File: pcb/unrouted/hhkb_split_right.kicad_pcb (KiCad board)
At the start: 2 copper layers, 173.7 x 97.4 mm, 83 parts, among them SW1 CPG151101S11-2, SW10 CPG151101S11-2, SW11 CPG151101S11-2, SW12 CPG151101S11-2, SW13 CPG151101S11-2, SW14 CPG151101S11-2, SW15 CPG151101S11-2, SW16 CPG151101S11-2, SW17 CPG151101S11-2, SW18 CPG151101S11-2, SW19 CPG151101S11-2, SW2 CPG151101S11-2, SW20 CPG151101S11-2, SW21 CPG151101S11-2, SW22 CPG151101S11-2, SW23 CPG151101S11-2, SW24 CPG151101S11-2, SW25 CPG151101S11-2, SW26 CPG151101S11-2, SW27 CPG151101S11-2, SW28 CPG151101S11-2, SW29 CPG151101S11-2, SW3 CPG151101S11-2, SW30 CPG151101S11-2, SW31 CPG151101S11-2, SW32 CPG151101S11-2, SW33 CPG151101S11-2, SW34 CPG151101S11-2, SW4 CPG151101S11-2, SW5 CPG151101S11-2, SW6 CPG151101S11-2, SW7 CPG151101S11-2, SW8 CPG151101S11-2, SW9 CPG151101S11-2, U1 74LVC595, U2 74LVC595

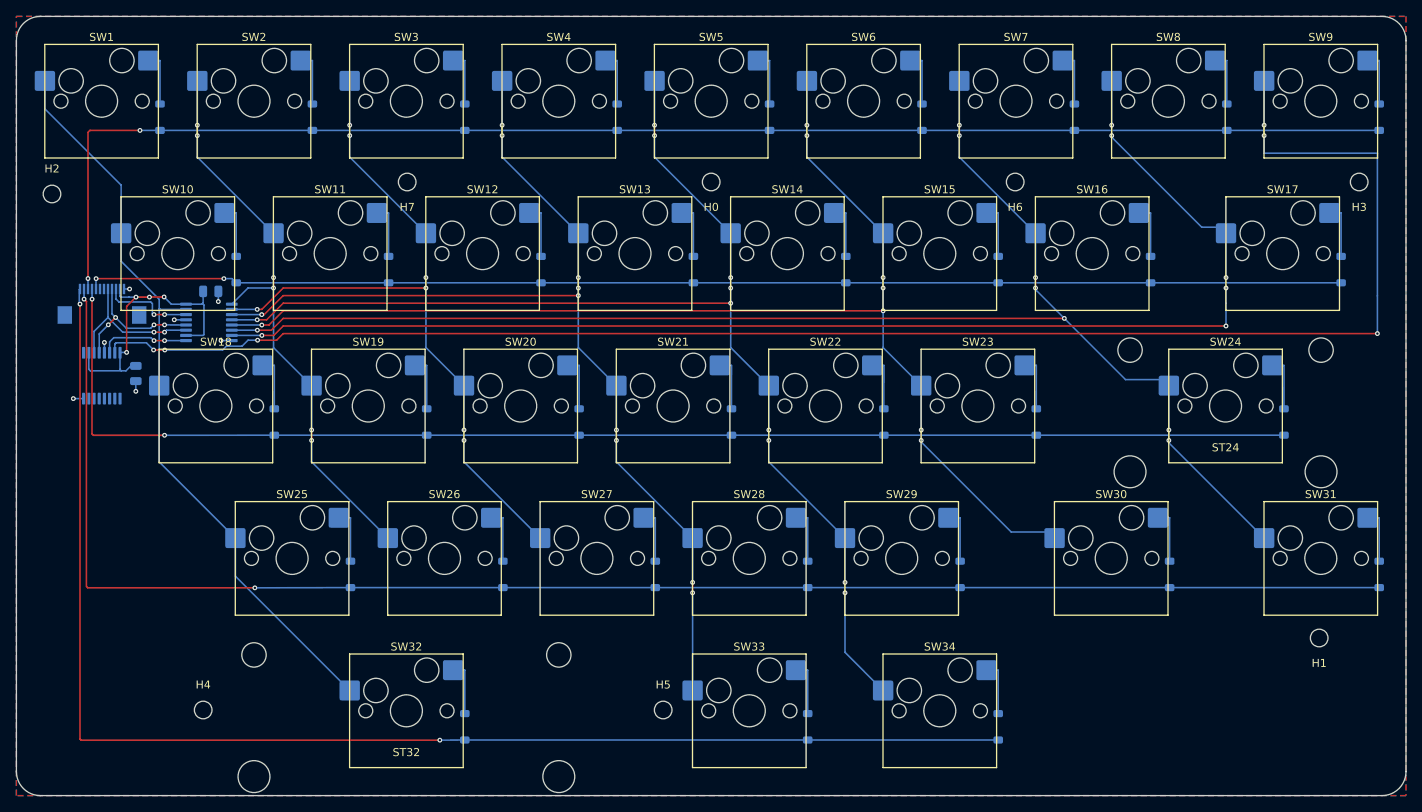
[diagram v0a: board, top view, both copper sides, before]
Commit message: #51 候補 3 を「右半分のみ」で実装した（PLATE_MARGIN_X_RIGHT = 3.125・幅 177.7mm）
利用者の採用決定を受けた実装。**左は実機のまま**——全幅で詰めると
電池（外壁基準）と子基板（内壁基準）が両側から近づき、左のアンテナ・
電池距離が 10.56→8.56mm で要件 10mm を割る（実装して発覚・巻き戻した）。
右の同距離は余裕 40mm で影響なし。実機からの逸脱も右半分だけになった。

- interface.py: 右専用余白＋margin_x()/margin_x_for_case()（キー幅 150mm/
  ケース幅 158mm を境に半分を判別。呼び出し元の変更を最小化）
- BEZEL_WALL 1.6→1.2・BEZEL_OPENING_GAP 1.5→0.9 は左右共通
  （見える隙間 1.225mm = 実機実測 1.0〜1.5 の範囲内）
- 検査: 余白の実機由来検査を左右別に・ベゼル幾何検査を両半分で実施・
  キャップ隙間の下限を実機実測の 1.0 に更新
- 右の新外形板を matrix_only に用意（利用者が J_DB 周り 9 ネットを引き直し中）
- 左基板・DRC 記録は凍結のまま無傷

検証: DRC 0/0/0（左右とも現行板で）・幾何/不変検査 138 件緑・
gen_assembly 左 干渉 0・全検査で残る赤は右基板系 3 件のみ
（旧外形の本番右板 vs 新定数。引き直し→finalize で解消する見込み）

Co-Authored-By: Claude Fable 5 <noreply@anthropic.com>
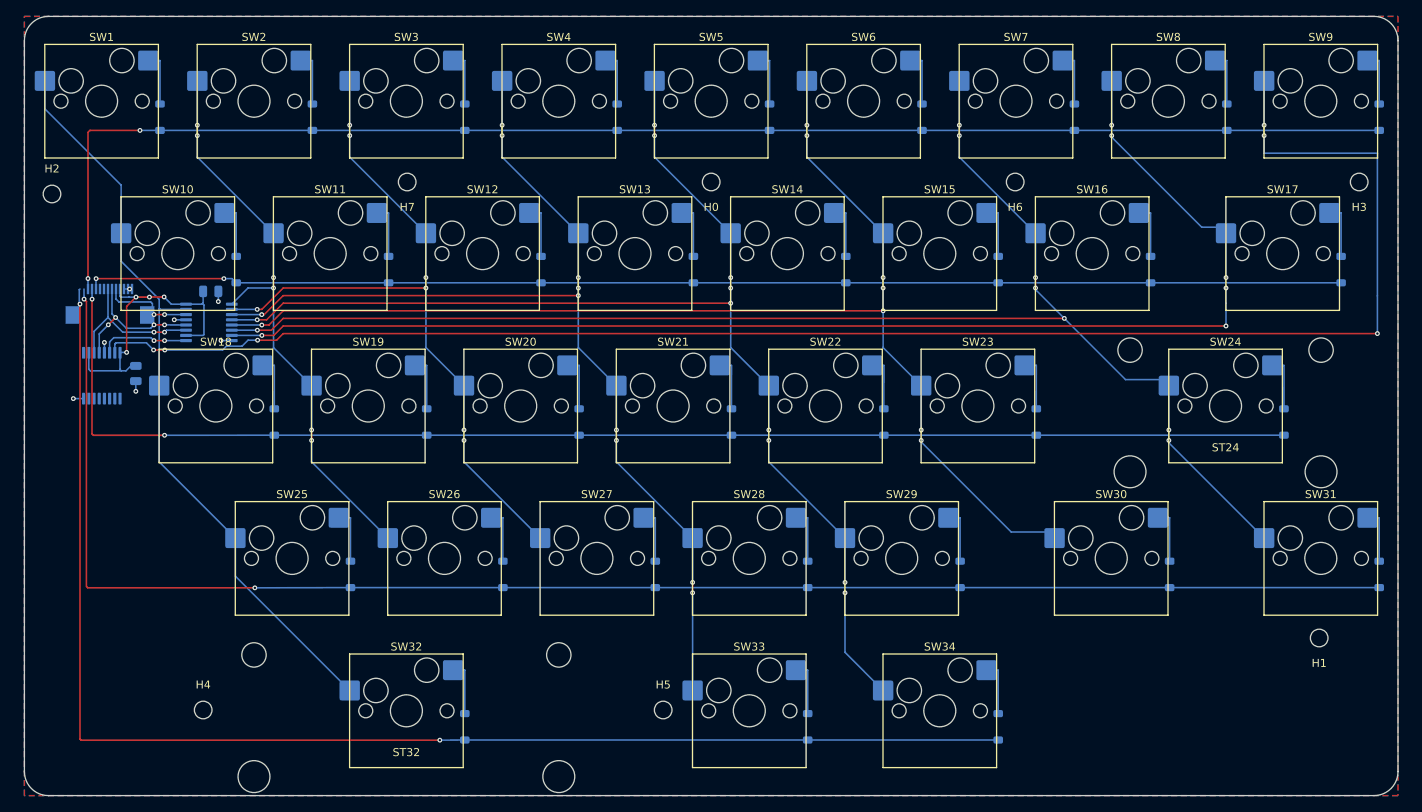
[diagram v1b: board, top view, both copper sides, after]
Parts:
- moved J_DB 1.00 mm to (74.8, 87.2)
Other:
- board size 173.7 x 97.4 mm -> 171.7 x 97.4 mm

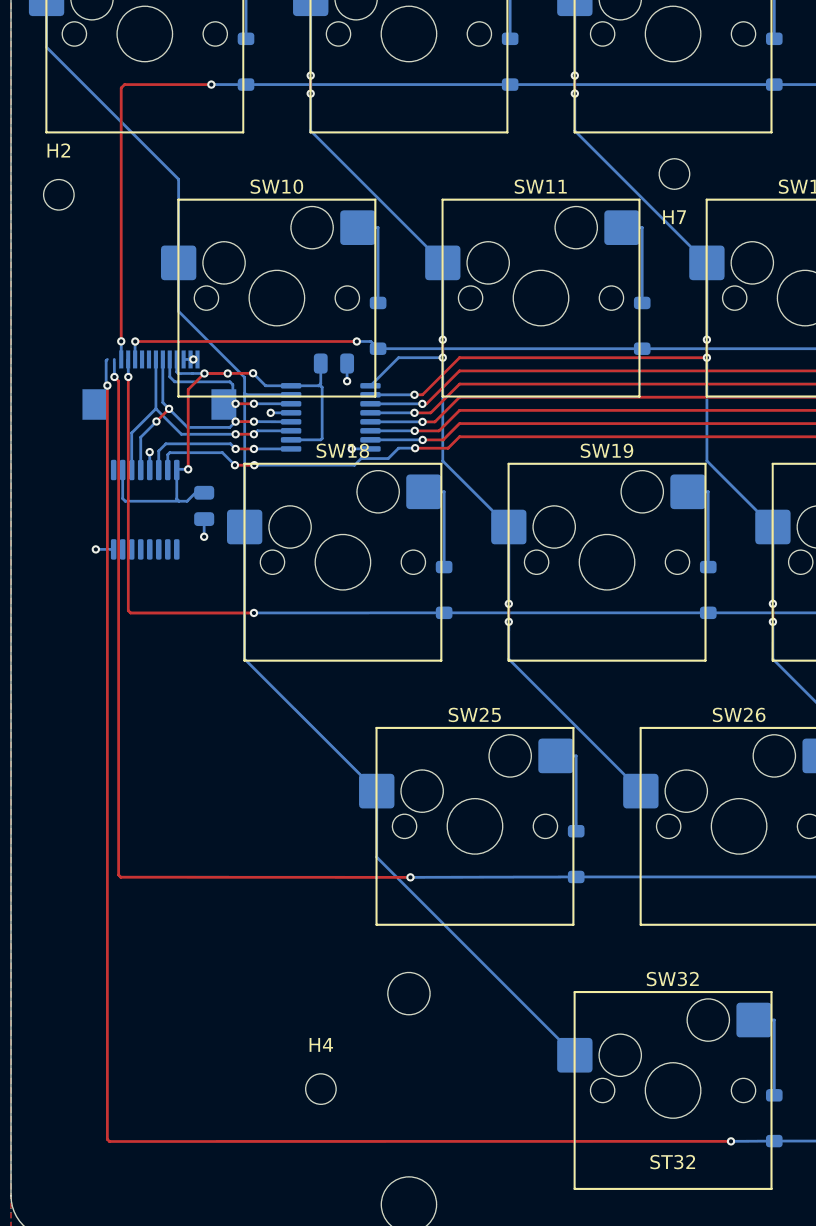
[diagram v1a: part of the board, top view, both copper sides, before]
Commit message: #51 の基板一式——3 枚とも DRC 違反 0 / 未配線 0
利用者が右の J_DB 周り 9 ネットを新しい位置へ引き直し（matrix_only）、
V3V3 の切れ目と、写しの φ0.5→0.56 化で近すぎたビア 3 ペアも修正。
写し（matrix_routing.json）→ gen_pcb（外形 左 138.4 / 右 171.7）→
finalize --src unrouted → DRC の全経路を通した。部品位置の写しを含む。

Co-Authored-By: Claude Fable 5 <noreply@anthropic.com>
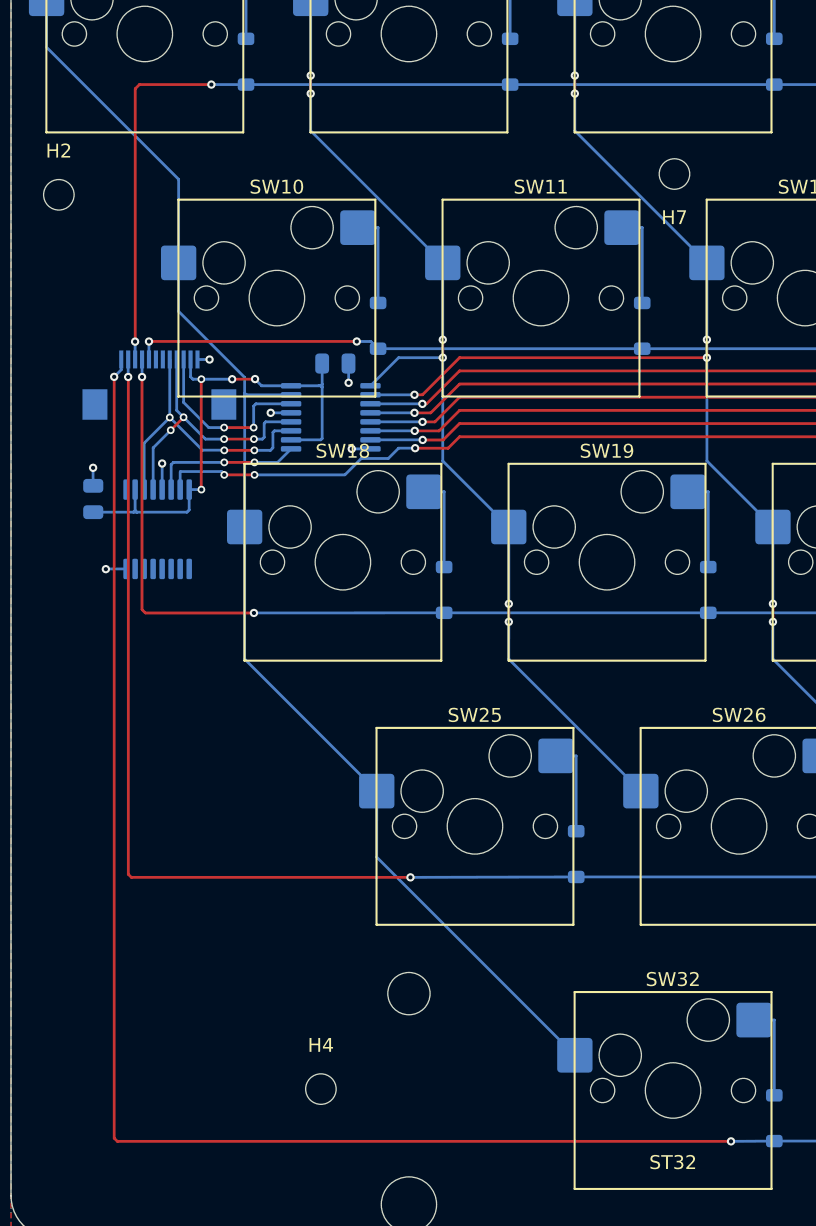
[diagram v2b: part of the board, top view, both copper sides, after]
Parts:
- moved C_U2 8.02 mm to (70.1, 95.4), turned to 90 degrees
- moved U2 1.67 mm to (74.7, 97.6)
- moved C_U1 0.10 mm to (87.5, 85.7)
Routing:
- net SPI_SCK: track 19.3 -> 21.3 mm, vias 2 -> 3
- net V3V3: track 40.0 -> 38.0 mm
- net SPI_MOSI: track 11.6 -> 13.2 mm
- net CS: track 18.5 -> 20.0 mm
- net GND: track 8.65 -> 9.74 mm
- net ROW_C: track 181.1 -> 180.0 mm
- net ROW_B: track 167.2 -> 166.1 mm
- net ROW_A: track 157.1 -> 156.1 mm
- net ROW_D: track 199.0 -> 198.1 mm
- net COL8: track 206.0 -> 205.1 mm

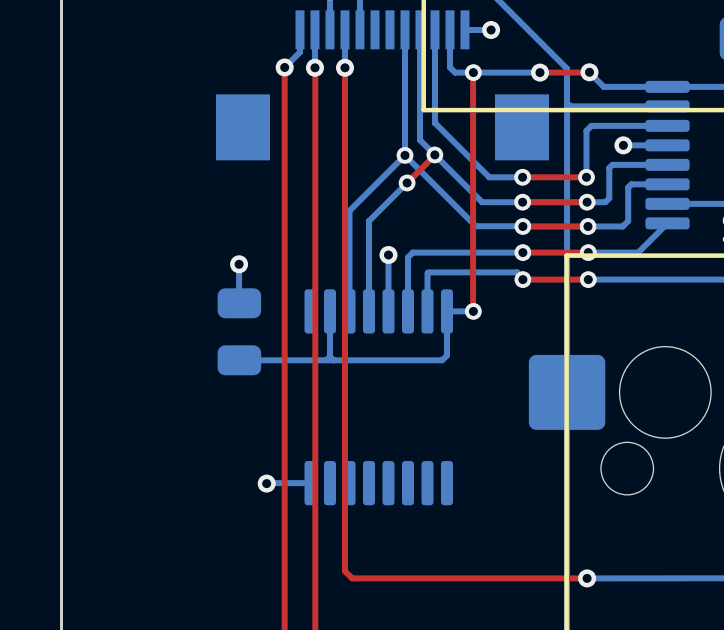
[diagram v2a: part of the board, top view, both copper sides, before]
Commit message: C_U2 の寄せ（利用者）を取り込み、番人 MAX_DECOUPLE_MM を根拠つきで 6.5 へ——**全検査 458 件緑**
利用者が C_U2 を U2 の干渉限界まで寄せ（7.11 → 6.21mm）シルクも修正。
上限 6.0 は「物理から決まらない・17mm 再発防止の番人」と自ら明記された
経験則なので、実配置 6.21 + 余裕 0.3 = 6.5 へ更新（全ペアの現状:
左 C_U1 4.97 / 右 C_U1 2.76 / 右 C_U2 6.21）。

これで #51 関連の作業は完了:
- 3 基板とも DRC 違反 0 / 未配線 0
- 実形状の組み立て干渉 左右 0
- 全検査 458 件緑・skip 9

Co-Authored-By: Claude Fable 5 <noreply@anthropic.com>
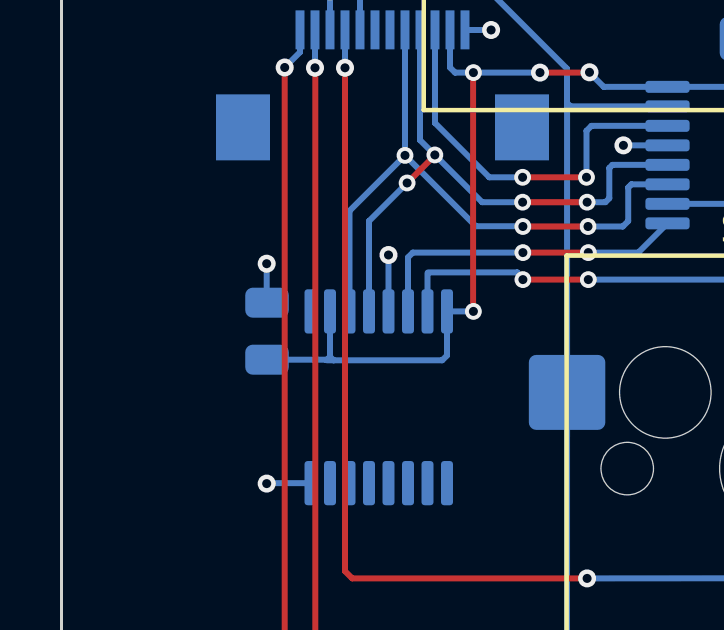
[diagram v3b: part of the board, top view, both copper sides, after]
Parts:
- moved C_U2 0.92 mm to (71.0, 95.4)
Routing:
- net V3V3: track 38.0 -> 37.1 mm

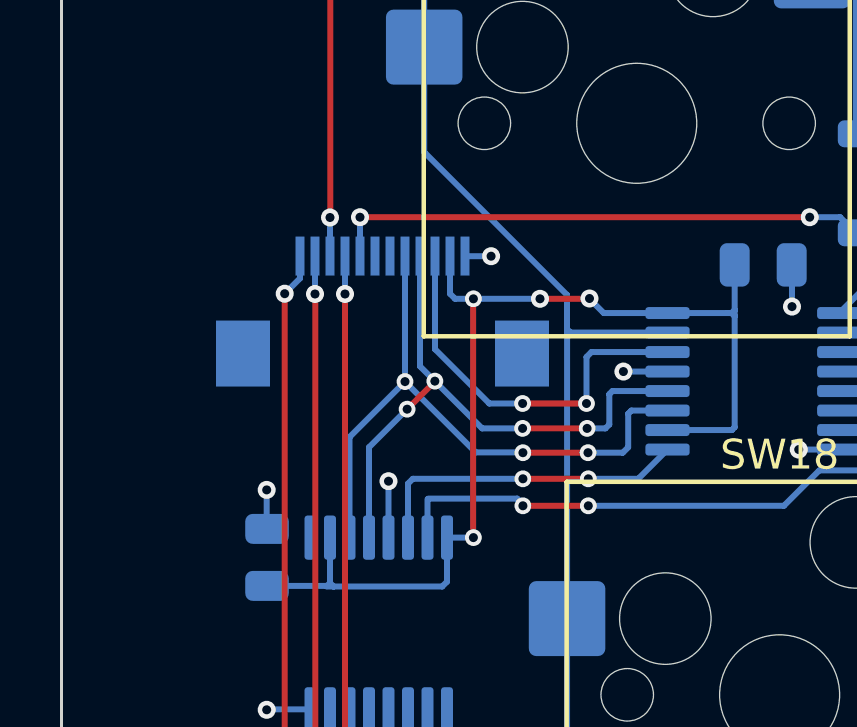
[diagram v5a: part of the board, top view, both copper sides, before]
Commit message: #19 J_DB の口を奥向きに回した（FFC は直線・A タイプで正しい）。左は配線無傷で DRC 0、右は J_DB 周りの引き直し待ち
- 原因: 2026-08-08 の初回配置で Flip() の副作用の 180° をそのまま使い、誰も口の向きを決めていなかった（git 履歴で確認）
- circuit.py: J_DB のピン表を J_MAIN の鏡像（n ↔ 13-n）に。裏面で 180° 回すとピン 1 の側が入れ替わるため。検査 2 本と決定文書を鏡像に更新
- gen_pcb.py: J_DB に向き 0° と dy（左 -3.7 / 右 -0.4）。配置は matrix_only の現物が優先
- 左 matrix_only: J_DB を 0°・3.7mm 奥へ → 12 パッドが同じ座標に戻り配線無傷。DRC 0/0
- 右 matrix_only: 3.7mm は SW10 の NPTH がコートヤードに入るため 0.4mm 止まり。パッドが南側の枝と重なり DRC 違反 20・未配線 8（利用者の引き直し・open-gaps #19 に手順）
- gen_assembly.py: 幕と床走行を消し、口の直後の潜り＋J_MAIN までの斜めのリボンに。箱モード干渉 0
- 回路図・部品記録・DRC 記録・証拠ページを更新。検査 455 緑・5 赤（全部右の引き直しと露出ビアの打ち直しに帰着・open-gaps に列挙）

Co-Authored-By: Claude Fable 5 <noreply@anthropic.com>
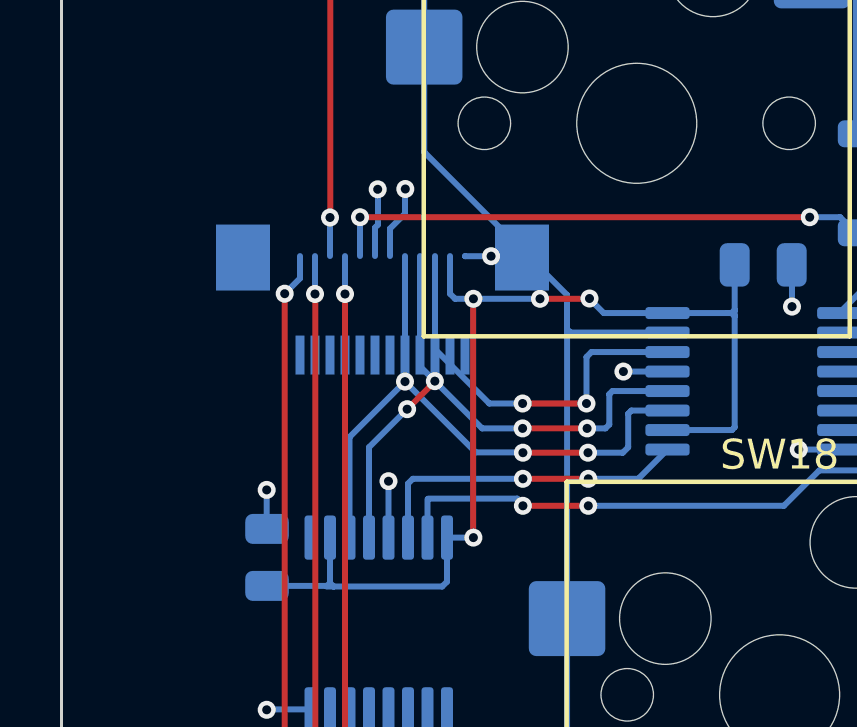
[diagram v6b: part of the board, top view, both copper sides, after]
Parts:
- moved J_DB 0.40 mm to (74.8, 86.8), turned to 0 degrees
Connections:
- J_DB pad 1: GND -> ROW_E
- J_DB pad 10: ROW_C -> SPI_MOSI
- J_DB pad 11: ROW_D -> V3V3
- J_DB pad 12: ROW_E -> GND
- J_DB pad 2: V3V3 -> ROW_D
- J_DB pad 3: SPI_MOSI -> ROW_C
- J_DB pad 4: CS -> ROW_B
- J_DB pad 5: SPI_SCK -> ROW_A
- J_DB pad 6: SPARE2 -> SPARE
- J_DB pad 7: SPARE -> SPARE2
- J_DB pad 8: ROW_A -> SPI_SCK
- J_DB pad 9: ROW_B -> CS
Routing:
- net SPARE2: track 0.00 -> 2.43 mm, vias 0 -> 1
- net SPARE: track 0.00 -> 2.27 mm, vias 0 -> 1

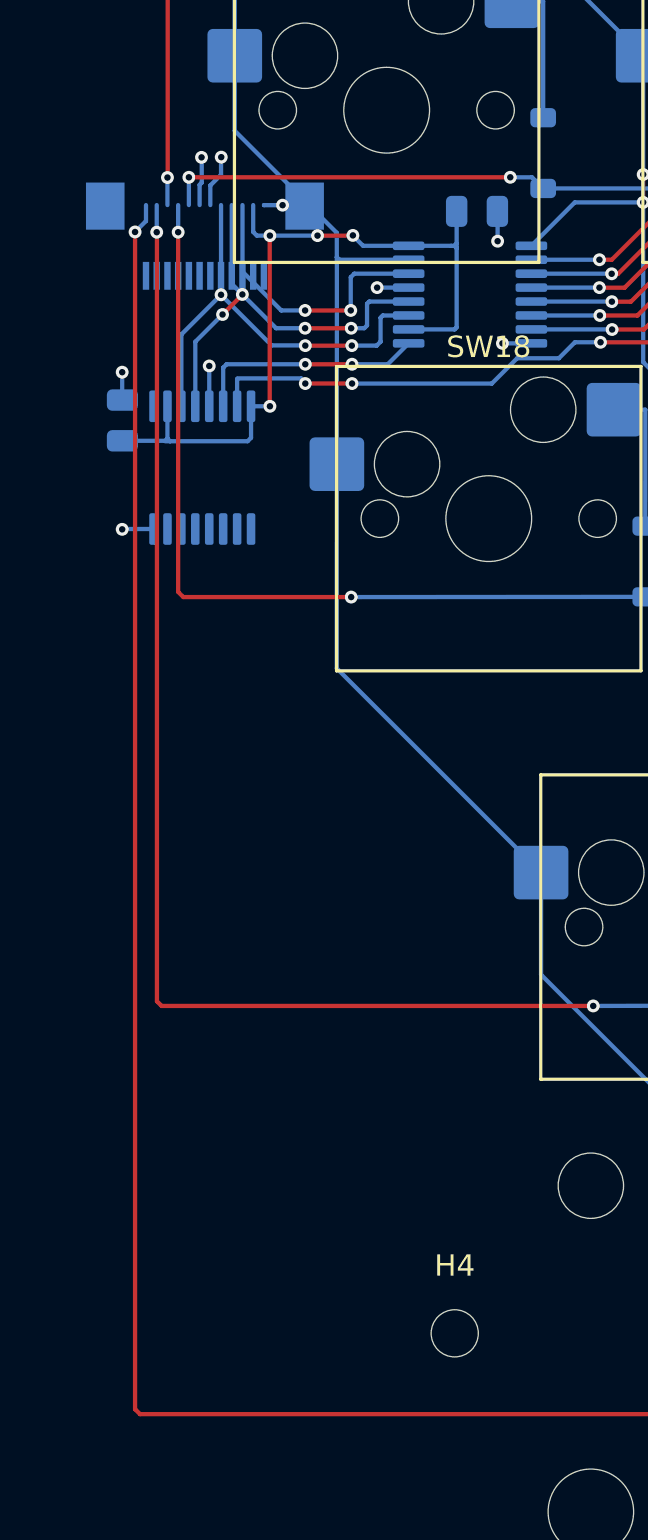
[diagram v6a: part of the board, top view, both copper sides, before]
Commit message: #19 右の J_DB 周りを利用者が引き直し、3 基板とも DRC 0 / 未配線 0
- COL0 の斜め線が回した J_DB の MP パッドを横切っていたのを MP の外（x=81 → y=82.3、SW10 の穴から 0.25mm 以上）へ逃がした
- φ0.5 の GND ビア 1 個を φ0.6 に
- 検査 457 緑・3 赤（右 J_DB とソケットの保守的占有範囲の重なり 1.63mm＝利用者の判断、露出ビアの打ち直し）。open-gaps #19 に記録
- 部品記録・DRC 記録・証拠ページを更新。gen_case.py の別セッションの変更は含めない

Co-Authored-By: Claude Fable 5 <noreply@anthropic.com>
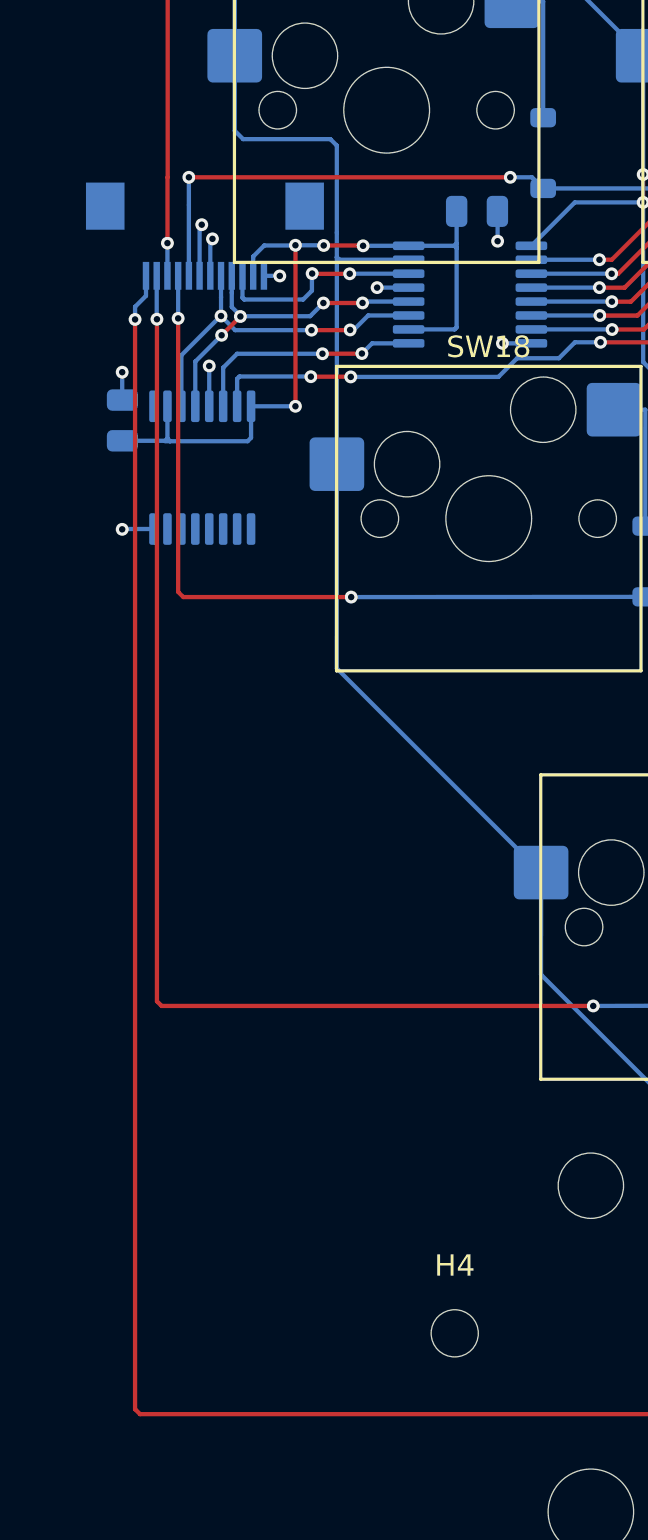
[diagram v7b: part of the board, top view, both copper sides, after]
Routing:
- net SPI_SCK: track 21.3 -> 16.1 mm
- net CS: track 20.0 -> 15.3 mm
- net SPI_MOSI: track 13.2 -> 9.74 mm
- net ROW_D: track 198.1 -> 194.8 mm
- net ROW_E: track 170.8 -> 167.5 mm
- net ROW_C: track 180.0 -> 183.3 mm
- net ROW_A: track 156.1 -> 159.4 mm
- net ROW_B: track 166.1 -> 162.8 mm
- net COL0: track 95.5 -> 97.9 mm
- net SPARE2: track 2.43 -> 1.77 mm

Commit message: #49 利用者が左右の露出ビア（SPARE/SPARE2）を打ち直し。右の COL0 迂回と GND ビア径を当て直し、3 基板とも DRC 0
- 左右とも SPARE/SPARE2 が露出できるようになった（左 SCK は未だ）
- ⚠️ 打った場所はコネクタの奥側＝ケーブルの通り道。南側への移動を提案（open-gaps #19）

Co-Authored-By: Claude Fable 5 <noreply@anthropic.com>
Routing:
- net SPARE2: track 1.77 -> 10.2 mm
- net SPARE: track 2.43 -> 10.5 mm
